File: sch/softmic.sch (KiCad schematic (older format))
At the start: 73 parts, among them J1 USB-C, J2 Conn_01x03, J3 XLR-OUT, P1 4V1, P2 4V1, P3 VccPad, Q1 MMBFJ201, Q2 BSS64AT116, SW1 SW_Push, SW2 SW_Push, U1 MCP1812BT-033, U2 MCP2221A, U3 OPA1671, U4 OPA1671, U5 BQ21040, U6 MAX11613, U7 Oled_128_32, U8 ESP32-WROOM

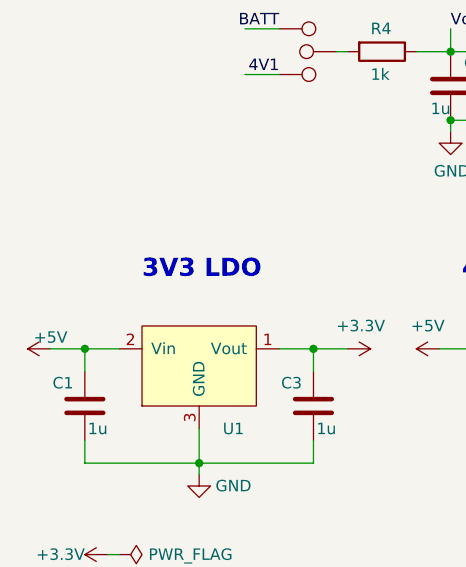
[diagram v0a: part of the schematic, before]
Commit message: in schematic, now LDO input can be USB 5V or internal battery
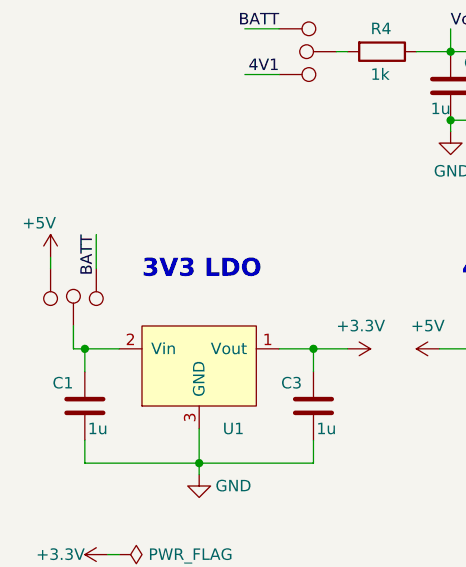
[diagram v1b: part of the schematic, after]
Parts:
- added P? (x3): 4V1, TestPoint:TestPoint_Pad_D1.0mm, symbol Connector:TestPoint
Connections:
- wire segments 216 -> 219
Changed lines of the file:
@@
 $EndComp
-Wire Wire Line
-	750  6550 900  6550
 Wire Wire Line
 	900  6650 900  6550
-Connection ~ 900  6550
 Wire Wire Line
 	900  6550 1050 6550
@@
 L power:+5V #PWR01
 U 1 1 5E8C4DF2
-P 750 6550
-F 0 "#PWR01" H 750 6400 50  0001 C CNN
-F 1 "+5V" V 700 6550 50  0000 C CNN
-F 2 "" H 750 6550 50  0001 C CNN
-F 3 "" H 750 6550 50  0001 C CNN
-	1    750  6550
-	0    -1   1    0
+P 750 6150
+F 0 "#PWR01" H 750 6000 50  0001 C CNN
+F 1 "+5V" H 800 6300 50  0000 C CNN
+F 2 "" H 750 6150 50  0001 C CNN
+F 3 "" H 750 6150 50  0001 C CNN
+	1    750  6150
+	-1   0    0    -1
 $EndComp
 Wire Wire Line
@@
 Wire Wire Line
 	7500 1300 8000 1300
+$Comp
+L Connector:TestPoint P?
+U 1 1 5E9C020B
+P 950 6200
+F 0 "P?" H 950 6250 50  0001 L CNN
+F 1 "4V1" V 1050 6200 50  0001 L CNN
+F 2 "TestPoint:TestPoint_Pad_D1.0mm" H 1150 6200 50  0001 C CNN
+F 3 "~" H 1150 6200 50  0001 C CNN
+F 4 "none" H 950 6200 50  0001 C CNN "Manufacturer"
+F 5 "none" H -2350 1900 50  0001 C CNN "MPN"
+F 6 "none" H 950 6200 50  0001 C CNN "Description"
+F 7 "none" H -2350 1900 50  0001 C CNN "Digikey PN"
+F 8 "none" H -2350 1900 50  0001 C CNN "Digikey Price"
+F 9 "none" H -2350 1900 50  0001 C CNN "Mouser PN"
+F 10 "none" H -2350 1900 50  0001 C CNN "Mouser Price"
+F 11 "none" H -2350 1900 50  0001 C CNN "LCSC PN"
+F 12 "none" H -2350 1900 50  0001 C CNN "LCSC Price"
+	1    950  6200
+	-1   0    0    1
+$EndComp
+Text Label 950  6050 3    50   ~ 0
+BATT
+Wire Wire Line
+	950  6200 950  6050
+$Comp
+L Connector:TestPoint P?
+U 1 1 5E9EA033
+P 750 6200
+F 0 "P?" H 750 6250 50  0001 L CNN
+F 1 "4V1" V 850 6200 50  0001 L CNN
+F 2 "TestPoint:TestPoint_Pad_D1.0mm" H 950 6200 50  0001 C CNN
+F 3 "~" H 950 6200 50  0001 C CNN
+F 4 "none" H 750 6200 50  0001 C CNN "Manufacturer"
+F 5 "none" H -2550 1900 50  0001 C CNN "MPN"
+F 6 "none" H 750 6200 50  0001 C CNN "Description"
+F 7 "none" H -2550 1900 50  0001 C CNN "Digikey PN"
+F 8 "none" H -2550 1900 50  0001 C CNN "Digikey Price"
+F 9 "none" H -2550 1900 50  0001 C CNN "Mouser PN"
+F 10 "none" H -2550 1900 50  0001 C CNN "Mouser Price"
+F 11 "none" H -2550 1900 50  0001 C CNN "LCSC PN"
+F 12 "none" H -2550 1900 50  0001 C CNN "LCSC Price"
+	1    750  6200
+	-1   0    0    1
+$EndComp
+$Comp
+L Connector:TestPoint P?
+U 1 1 5E9F84C4
+P 850 6450
+F 0 "P?" H 850 6500 50  0001 L CNN
+F 1 "4V1" V 950 6450 50  0001 L CNN
+F 2 "TestPoint:TestPoint_Pad_D1.0mm" H 1050 6450 50  0001 C CNN
+F 3 "~" H 1050 6450 50  0001 C CNN
+F 4 "none" H 850 6450 50  0001 C CNN "Manufacturer"
+F 5 "none" H -2450 2150 50  0001 C CNN "MPN"
+F 6 "none" H 850 6450 50  0001 C CNN "Description"
+F 7 "none" H -2450 2150 50  0001 C CNN "Digikey PN"
+F 8 "none" H -2450 2150 50  0001 C CNN "Digikey Price"
+F 9 "none" H -2450 2150 50  0001 C CNN "Mouser PN"
+F 10 "none" H -2450 2150 50  0001 C CNN "Mouser Price"
+F 11 "none" H -2450 2150 50  0001 C CNN "LCSC PN"
+F 12 "none" H -2450 2150 50  0001 C CNN "LCSC Price"
+	1    850  6450
+	1    0    0    -1
+$EndComp
+Wire Wire Line
+	900  6550 850  6550
+Connection ~ 900  6550
+Wire Wire Line
+	750  6150 750  6200
+Wire Wire Line
+	850  6450 850  6550
 $EndSCHEMATC

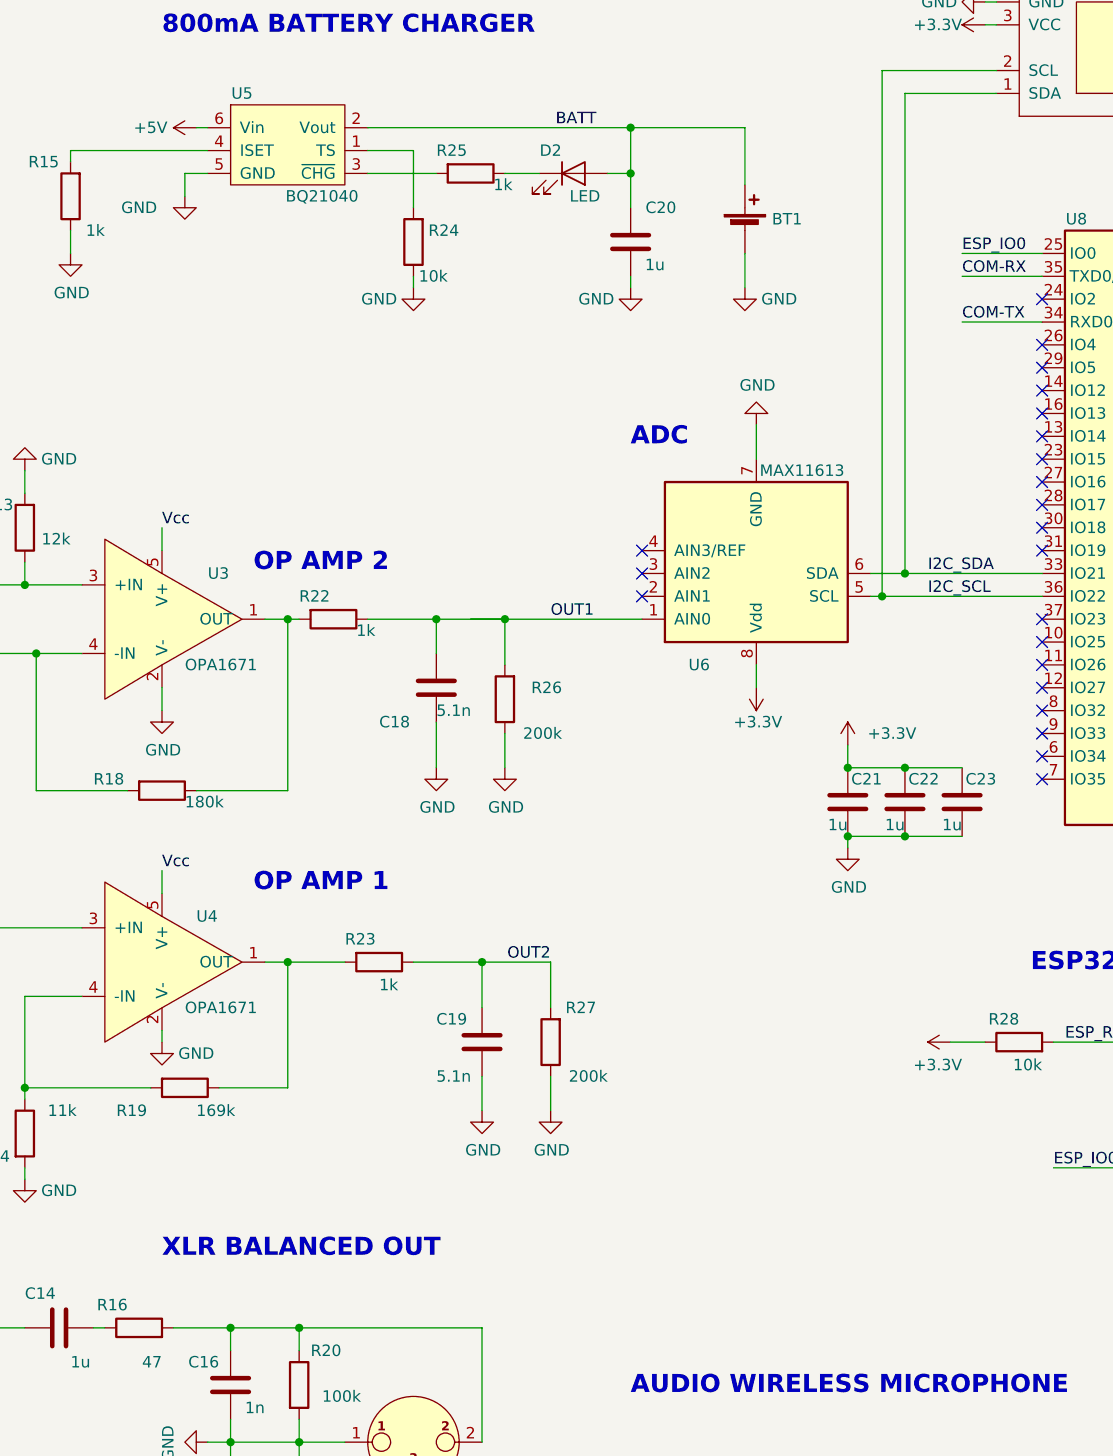
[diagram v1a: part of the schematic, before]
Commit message: added line out audio jack in schematic and PCB
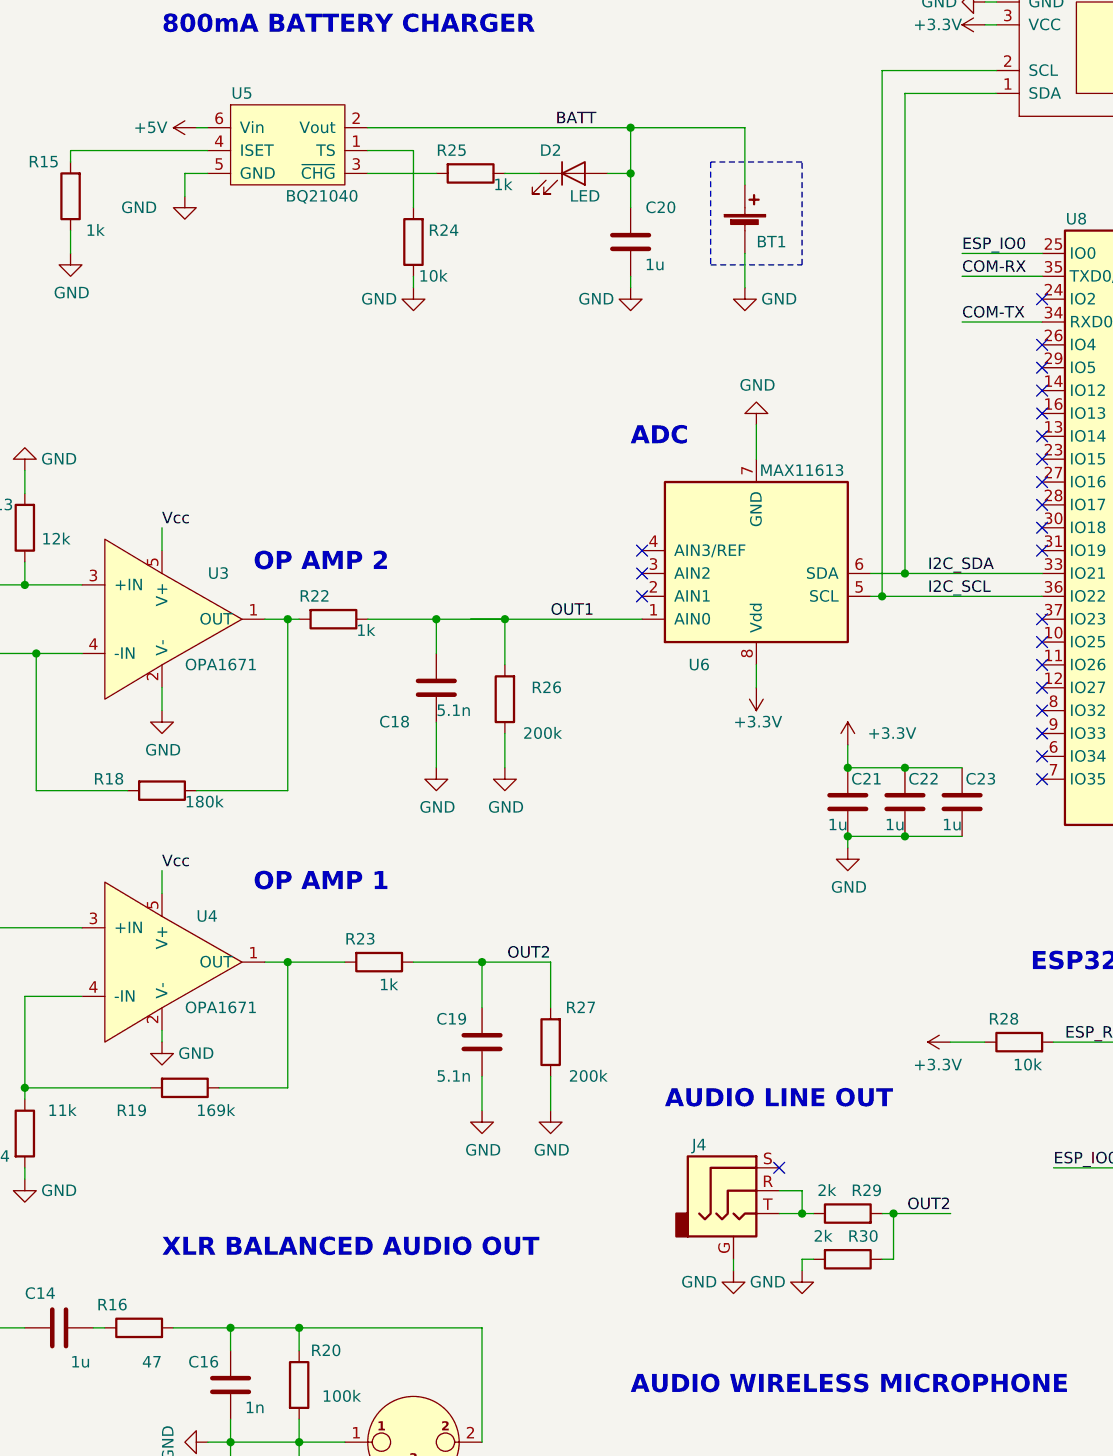
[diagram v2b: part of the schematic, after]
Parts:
- added J4: AudioJack3_Ground, footprint:SJ-43514-SM, symbol Connector:AudioJack3_Ground
- added R29, R30: 2k, Resistor_SMD:R_0603_1608Metric, symbol Device:R
- BT1: value Battery_Cell -> 1-Cell Litium Battery
- gave numbers to parts that had none: 3
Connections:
- wire segments 219 -> 230
- no-connect marks 42 -> 43
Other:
- note added: "AUDIO LINE OUT\n"
- note added: "XLR BALANCED AUDIO OUT\n"
- note removed: "XLR BALANCED OUT\n"
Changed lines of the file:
@@
 $EndComp
 Text Notes 5450 6250 0    79   ~ 16
-XLR BALANCED OUT\n
+XLR BALANCED AUDIO OUT\n
 $Comp
 L OPA1671:OPA1671 U4
@@
 U 1 1 5E8AE25F
 P 8000 1750
-F 0 "BT1" H 8118 1800 50  0000 L CNN
-F 1 "Battery_Cell" H 8118 1755 50  0001 L CNN
+F 0 "BT1" H 8050 1700 50  0000 L CNN
+F 1 "1-Cell Litium Battery" H 8118 1755 50  0001 L CNN
 F 2 "Battery:BatteryHolder_Keystone_1042_1x18650" V 8000 1810 50  0001 C CNN
 F 3 "~" V 8000 1810 50  0001 C CNN
@@
 	7500 1300 8000 1300
 $Comp
-L Connector:TestPoint P?
+L Connector:TestPoint P6
 U 1 1 5E9C020B
 P 950 6200
-F 0 "P?" H 950 6250 50  0001 L CNN
+F 0 "P6" H 950 6250 50  0001 L CNN
 F 1 "4V1" V 1050 6200 50  0001 L CNN
 F 2 "TestPoint:TestPoint_Pad_D1.0mm" H 1150 6200 50  0001 C CNN
@@
 	950  6200 950  6050
 $Comp
-L Connector:TestPoint P?
+L Connector:TestPoint P4
 U 1 1 5E9EA033
 P 750 6200
-F 0 "P?" H 750 6250 50  0001 L CNN
+F 0 "P4" H 750 6250 50  0001 L CNN
 F 1 "4V1" V 850 6200 50  0001 L CNN
 F 2 "TestPoint:TestPoint_Pad_D1.0mm" H 950 6200 50  0001 C CNN
@@
 $EndComp
 $Comp
-L Connector:TestPoint P?
+L Connector:TestPoint P5
 U 1 1 5E9F84C4
 P 850 6450
-F 0 "P?" H 850 6500 50  0001 L CNN
+F 0 "P5" H 850 6500 50  0001 L CNN
 F 1 "4V1" V 950 6450 50  0001 L CNN
 F 2 "TestPoint:TestPoint_Pad_D1.0mm" H 1050 6450 50  0001 C CNN
@@
 Wire Wire Line
 	850  6450 850  6550
+$Comp
+L Connector:AudioJack3_Ground J4
+U 1 1 5EA40DAB
+P 7950 5950
+F 0 "J4" H 7800 6150 50  0000 C CNN
+F 1 "AudioJack3_Ground" H 7932 6184 50  0001 C CNN
+F 2 "footprint:SJ-43514-SM" H 7950 5950 50  0001 C CNN
+F 3 "~" H 7950 5950 50  0001 C CNN
+	1    7950 5950
+	1    0    0    -1
+$EndComp
+Text Notes 7650 5600 0    79   ~ 16
+AUDIO LINE OUT\n
+$Comp
+L power:GND #PWR052
+U 1 1 5EA42E13
+P 7950 6300
+F 0 "#PWR052" H 7950 6050 50  0001 C CNN
+F 1 "GND" H 7800 6250 50  0000 C CNN
+F 2 "" H 7950 6300 50  0001 C CNN
+F 3 "" H 7950 6300 50  0001 C CNN
+	1    7950 6300
+	1    0    0    -1
+$EndComp
+Wire Wire Line
+	7950 6250 7950 6300
+Wire Wire Line
+	8150 6050 8250 6050
+NoConn ~ 8150 5850
+Wire Wire Line
+	8150 5950 8250 5950
+Wire Wire Line
+	8250 5950 8250 6050
+Connection ~ 8250 6050
+Wire Wire Line
+	8250 6050 8300 6050
+Text Label 8900 6050 2    50   ~ 0
+OUT2
+$Comp
+L Device:R R29
+U 1 1 5EA8B4EC
+P 8450 6050
+F 0 "R29" V 8550 5900 50  0000 L CNN
+F 1 "2k" V 8550 6100 50  0000 L CNN
+F 2 "Resistor_SMD:R_0603_1608Metric" V 8380 6050 50  0001 C CNN
+F 3 "~" H 8450 6050 50  0001 C CNN
+F 4 "none" H 8450 6050 50  0001 C CNN "Manufacturer"
+F 5 "none" H 8450 6050 50  0001 C CNN "MPN"
+F 6 "RES SMD 2K OHM 1% 1/10W 0603" H 8450 6050 50  0001 C CNN "Description"
+F 7 "311-2.00KHRCT-ND" H 8450 6050 50  0001 C CNN "Digikey PN"
+F 8 "$0.10" H 8450 6050 50  0001 C CNN "Digikey Price"
+F 9 "603-RC0603FR-072KL" H 8450 6050 50  0001 C CNN "Mouser PN"
+F 10 "$0.10" H 8450 6050 50  0001 C CNN "Mouser Price"
+F 11 "C163892" H 8450 6050 50  0001 C CNN "LCSC PN"
+F 12 "$0.001847" H 8450 6050 50  0001 C CNN "LCSC Price"
+	1    8450 6050
+	0    -1   -1   0
+$EndComp
+Wire Wire Line
+	8600 6050 8650 6050
+$Comp
+L Device:R R30
+U 1 1 5EAB823C
+P 8450 6250
+F 0 "R30" V 8350 6250 50  0000 L CNN
+F 1 "2k" V 8350 6100 50  0000 L CNN
+F 2 "Resistor_SMD:R_0603_1608Metric" V 8380 6250 50  0001 C CNN
+F 3 "~" H 8450 6250 50  0001 C CNN
+F 4 "none" H 8450 6250 50  0001 C CNN "Manufacturer"
+F 5 "none" H 8450 6250 50  0001 C CNN "MPN"
+F 6 "RES SMD 2K OHM 1% 1/10W 0603" H 8450 6250 50  0001 C CNN "Description"
+F 7 "311-2.00KHRCT-ND" H 8450 6250 50  0001 C CNN "Digikey PN"
+F 8 "$0.10" H 8450 6250 50  0001 C CNN "Digikey Price"
+F 9 "603-RC0603FR-072KL" H 8450 6250 50  0001 C CNN "Mouser PN"
+F 10 "$0.10" H 8450 6250 50  0001 C CNN "Mouser Price"
+F 11 "C163892" H 8450 6250 50  0001 C CNN "LCSC PN"
+F 12 "$0.001847" H 8450 6250 50  0001 C CNN "LCSC Price"
+	1    8450 6250
+	0    1    1    0
+$EndComp
+Wire Wire Line
+	8650 6250 8650 6050
+Connection ~ 8650 6050
+Wire Wire Line
+	8650 6050 8900 6050
+Wire Wire Line
+	8600 6250 8650 6250
+Wire Wire Line
+	8300 6250 8250 6250
+$Comp
+L power:GND #PWR053
+U 1 1 5EB092F6
+P 8250 6300
+F 0 "#PWR053" H 8250 6050 50  0001 C CNN
+F 1 "GND" H 8100 6250 50  0000 C CNN
+F 2 "" H 8250 6300 50  0001 C CNN
+F 3 "" H 8250 6300 50  0001 C CNN
+	1    8250 6300
+	1    0    0    -1
+$EndComp
+Wire Wire Line
+	8250 6250 8250 6300
+Wire Notes Line
+	7850 1900 8250 1900
+Wire Notes Line
+	8250 1900 8250 1450
+Wire Notes Line
+	8250 1450 7850 1450
+Wire Notes Line
+	7850 1450 7850 1900
 $EndSCHEMATC
